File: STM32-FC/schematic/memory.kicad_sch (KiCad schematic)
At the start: 9 parts, among them J4 TF-06A, U5 W25X40CLUXIG

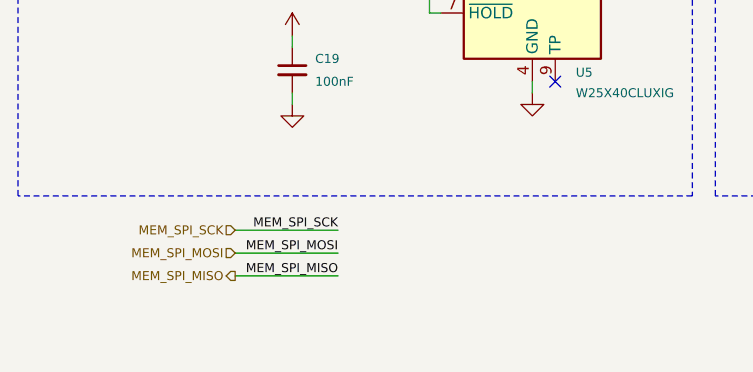
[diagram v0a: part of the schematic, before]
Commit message: v1.0.1 update WIP
repactor and USB C bug fix
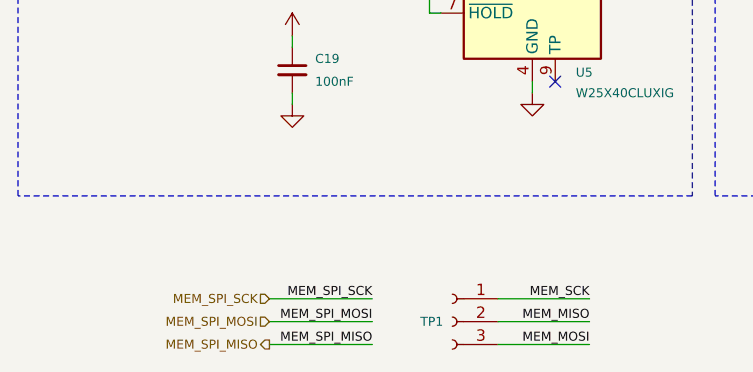
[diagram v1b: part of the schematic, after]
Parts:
- added TP1: Test Pin, Connector_PinHeader_1.27mm:PinHeader_1x03_P1.27mm_Vertical, symbol Connector:Conn_01x03_Socket
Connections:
- new net MEM_MISO: TP1.2 (Pin_2)
- new net MEM_MOSI: TP1.3 (Pin_3)
- new net MEM_SCK: TP1.1 (Pin_1)

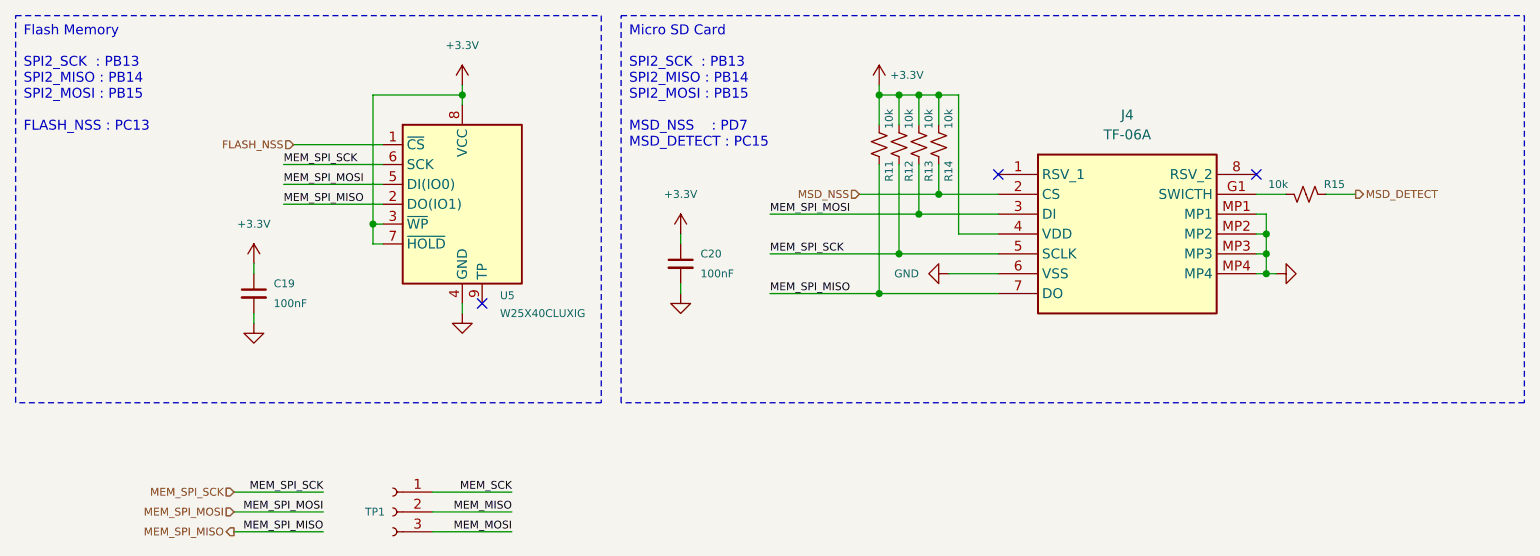
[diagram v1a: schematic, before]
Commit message: schematic update & lib update
- ICM-45686
- ICP-20100
- Micro SD update SDIO instead of SPI
- servo main output
- DC2DC buck instead power regulator
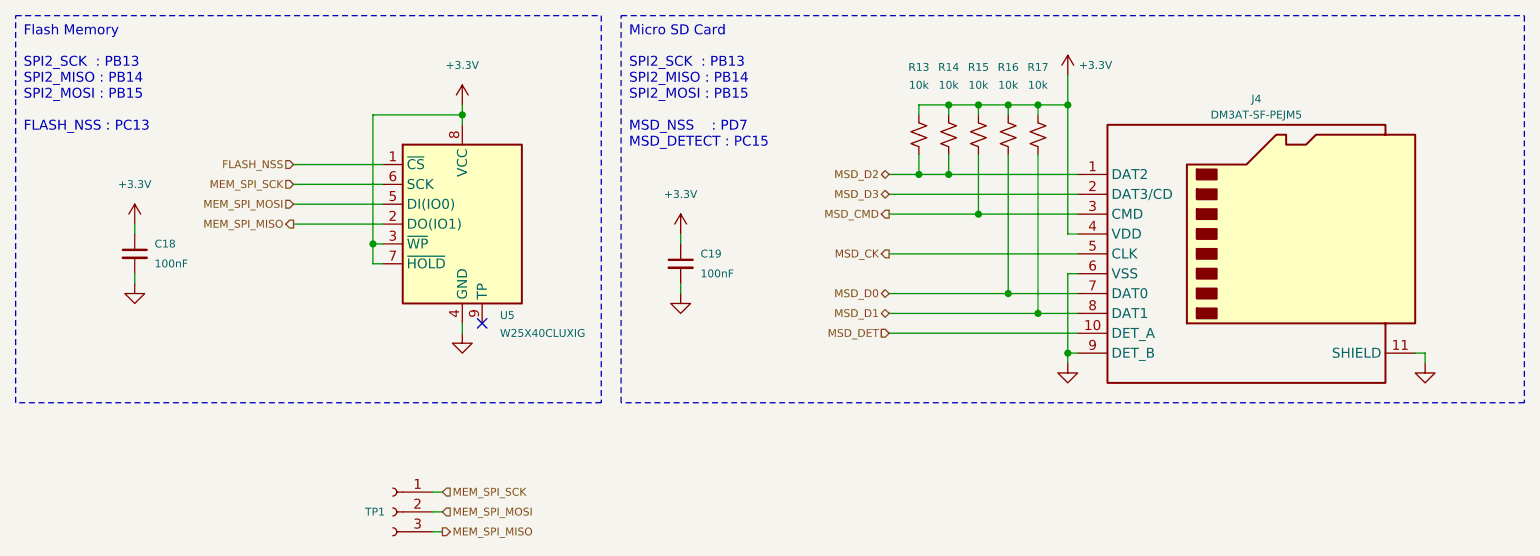
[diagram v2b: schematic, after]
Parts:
- removed J4: TF-06A, TF06A, symbol TF-06A:TF-06A
- removed R11, R12: 10k, Resistor_SMD:R_0402_1005Metric, symbol Device:R_Small_US
- added J4: DM3AT-SF-PEJM5, Connector_Card:microSD_HC_Hirose_DM3AT-SF-PEJM5, symbol Connector:Micro_SD_Card_Det2
- added R16, R17: 10k, Resistor_SMD:R_0402_1005Metric, symbol Device:R_Small_US
- U5: footprint W25X40CLUX:USON_LUXIG TR_WIN-L -> W25X40CLUX:USON_LUXIG_TR_HandSolder
- renumbered C19 to C18, C20 to C19
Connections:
- net MEM_MISO is gone; now on net MEM_SPI_MOSI: TP1.2 (Pin_2)
- net MEM_MOSI is gone; now on net MEM_SPI_MISO: TP1.3 (Pin_3)
- net MEM_SCK is gone; now on net MEM_SPI_SCK: TP1.1 (Pin_1)
- net MSD_DETECT is gone; now on net +3.3V: R15.1
- net +3.3V: now also J4.4 (VDD), R16.1, R17.1
- net GND: now also J4.11 (SHIELD), J4.6 (VSS), J4.9 (DET_B)
- net MEM_SPI_MOSI: no longer R13.2
- net MSD_CMD: now reaches R15.2
- net MSD_CMD: now also J4.3 (CMD)
- net MSD_NSS renamed MSD_D2
- net MSD_D2: now also R13.2, J4.1 (DAT2)
- new net MSD_CK: J4.5 (CLK)
- new net MSD_D0: J4.7 (DAT0), R16.2
- new net MSD_D1: J4.8 (DAT1), R17.2
- new net MSD_D3: J4.2 (DAT3/CD)
- new net MSD_DET: J4.10 (DET_A)
- no-connect marks 3 -> 1
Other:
- title: STM32 Flight Controller -> NARAEON - Flight Controller
- moved on the sheet: C18, U5

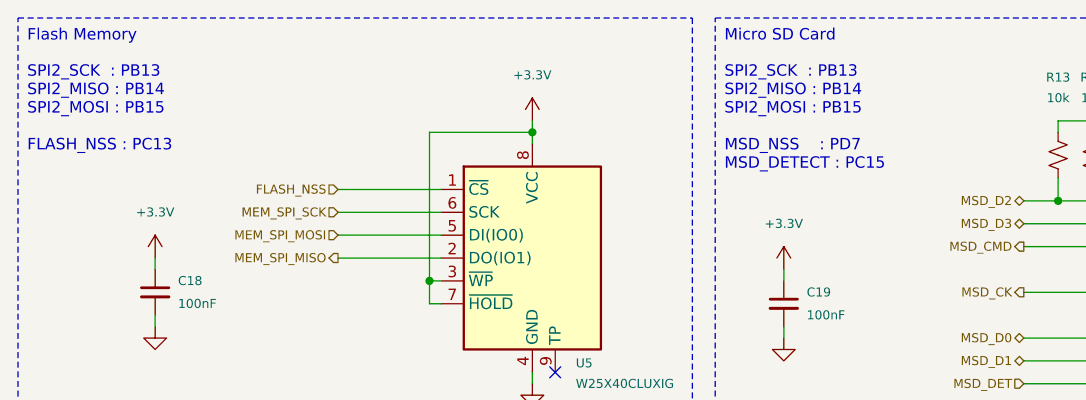
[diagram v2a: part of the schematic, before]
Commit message: add: servo power & comment
- Servo power diode add
- comment update
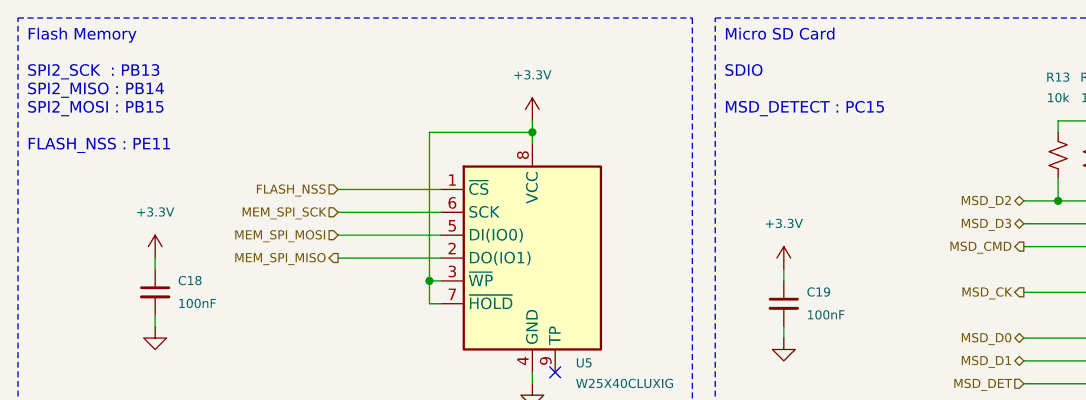
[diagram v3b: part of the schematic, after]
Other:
- note added: "SDIO MSD_DETECT : PC15"
- note added: "SPI2_SCK : PB13 SPI2_MISO : PB14 SPI2_MOSI : PB15 FLASH_NSS : PE11"
- note removed: "SPI2_SCK : PB13 SPI2_MISO : PB14 SPI2_MOSI : PB15 FLASH_NSS : PC13"
- note removed: "SPI2_SCK : PB13 SPI2_MISO : PB14 SPI2_MOSI : PB15 MSD_NSS : PD7 MSD_DETECT : PC15"
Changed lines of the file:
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@@
 	(title_block
 		(title "NARAEON - Flight Controller")
-		(date "2025-10-09")
+		(date "2025-10-10")
 		(rev "v1.1.0")
 		(company "NARAE")
@@
 		)
 	)
-	(text "SPI2_SCK  : PB13\nSPI2_MISO : PB14\nSPI2_MOSI : PB15\n\nMSD_NSS    : PD7\nMSD_DETECT : PC15"
+	(text "SDIO\n\nMSD_DETECT : PC15"
 		(exclude_from_sim no)
 		(at 101.346 18.034 0)
@@
 		)
 	)
-	(text "SPI2_SCK  : PB13\nSPI2_MISO : PB14\nSPI2_MOSI : PB15\n\nFLASH_NSS : PC13"
+	(text "SPI2_SCK  : PB13\nSPI2_MISO : PB14\nSPI2_MOSI : PB15\n\nFLASH_NSS : PE11"
 		(exclude_from_sim no)
 		(at 23.876 18.034 0)
@@
 		(dnp no)
 		(fields_autoplaced yes)
-		(property "Reference" "#PWR050"
+		(property "Reference" "#PWR053"
 			(at 157.48 63.5 0)
 			(effects
@@
 			(project "STM32-FC"
 				(path "/8d4cc317-3933-4aa6-844b-8c5c635e89c7/3e7c6c79-bc31-4cc9-af6a-d0a28245a7b2"
-					(reference "#PWR050")
+					(reference "#PWR053")
 					(unit 1)
 				)
@@
 		(dnp no)
 		(fields_autoplaced yes)
-		(property "Reference" "#PWR043"
+		(property "Reference" "#PWR046"
 			(at 38.1 43.18 0)
 			(effects
@@
 			(project "STM32-FC"
 				(path "/8d4cc317-3933-4aa6-844b-8c5c635e89c7/3e7c6c79-bc31-4cc9-af6a-d0a28245a7b2"
-					(reference "#PWR043")
+					(reference "#PWR046")
 					(unit 1)
 				)
@@
 		(dnp no)
 		(fields_autoplaced yes)
-		(property "Reference" "#PWR048"
+		(property "Reference" "#PWR051"
 			(at 107.95 54.61 0)
 			(effects
@@
 			(project "STM32-FC"
 				(path "/8d4cc317-3933-4aa6-844b-8c5c635e89c7/3e7c6c79-bc31-4cc9-af6a-d0a28245a7b2"
-					(reference "#PWR048")
+					(reference "#PWR051")
 					(unit 1)
 				)
@@
 		(dnp no)
 		(fields_autoplaced yes)
-		(property "Reference" "#PWR044"
+		(property "Reference" "#PWR047"
 			(at 38.1 53.34 0)
 			(effects
@@
 			(project "STM32-FC"
 				(path "/8d4cc317-3933-4aa6-844b-8c5c635e89c7/3e7c6c79-bc31-4cc9-af6a-d0a28245a7b2"
-					(reference "#PWR044")
+					(reference "#PWR047")
 					(unit 1)
 				)
@@
 		(dnp no)
 		(fields_autoplaced yes)
-		(property "Reference" "#PWR051"
+		(property "Reference" "#PWR054"
 			(at 203.2 63.5 0)
 			(effects
@@
 			(project "STM32-FC"
 				(path "/8d4cc317-3933-4aa6-844b-8c5c635e89c7/3e7c6c79-bc31-4cc9-af6a-d0a28245a7b2"
-					(reference "#PWR051")
+					(reference "#PWR054")
 					(unit 1)
 				)
@@
 		(dnp no)
 		(fields_autoplaced yes)
-		(property "Reference" "#PWR047"
+		(property "Reference" "#PWR050"
 			(at 107.95 44.45 0)
 			(effects
@@
 			(project "STM32-FC"
 				(path "/8d4cc317-3933-4aa6-844b-8c5c635e89c7/3e7c6c79-bc31-4cc9-af6a-d0a28245a7b2"
-					(reference "#PWR047")
+					(reference "#PWR050")
 					(unit 1)
 				)
@@
 		(on_board yes)
 		(dnp no)
-		(property "Reference" "#PWR049"
+		(property "Reference" "#PWR052"
 			(at 157.48 24.13 0)
 			(effects
@@
 			(project "STM32-FC"
 				(path "/8d4cc317-3933-4aa6-844b-8c5c635e89c7/3e7c6c79-bc31-4cc9-af6a-d0a28245a7b2"
-					(reference "#PWR049")
+					(reference "#PWR052")
 					(unit 1)
 				)
@@
 		(dnp no)
 		(fields_autoplaced yes)
-		(property "Reference" "#PWR045"
+		(property "Reference" "#PWR048"
 			(at 80.01 27.94 0)
 			(effects
@@
 			(project "STM32-FC"
 				(path "/8d4cc317-3933-4aa6-844b-8c5c635e89c7/3e7c6c79-bc31-4cc9-af6a-d0a28245a7b2"
-					(reference "#PWR045")
+					(reference "#PWR048")
 					(unit 1)
 				)
@@
 		(dnp no)
 		(fields_autoplaced yes)
-		(property "Reference" "#PWR046"
+		(property "Reference" "#PWR049"
 			(at 80.01 59.69 0)
 			(effects
@@
 			(project "STM32-FC"
 				(path "/8d4cc317-3933-4aa6-844b-8c5c635e89c7/3e7c6c79-bc31-4cc9-af6a-d0a28245a7b2"
-					(reference "#PWR046")
+					(reference "#PWR049")
 					(unit 1)
 				)

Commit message: WIP : pcb part layout &* BOM udpate
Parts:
- U5: footprint W25X40CLUX:USON_LUXIG_TR_HandSolder -> W25X40CLUX:USON_LUXIG TR_WIN
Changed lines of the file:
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@@
 			)
 		)
-		(property "Footprint" "W25X40CLUX:USON_LUXIG_TR_HandSolder"
+		(property "Footprint" "W25X40CLUX:USON_LUXIG TR_WIN"
 			(at 80.01 39.37 0)
 			(effects
@@
 			)
 		)
-		(property "Datasheet" "kicad-embed://w25x40cl_f 20140325.pdf"
+		(property "Datasheet" ""
 			(at 80.01 39.37 0)
 			(effects

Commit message: update : AHRS PCB layout & routing done
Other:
- note added: "SPI3_SCK : PB3 SPI3_MISO : PB4 SPI3_MOSI : PB5 FLASH_NSS : PE11"
- note removed: "SPI2_SCK : PB13 SPI2_MISO : PB14 SPI2_MOSI : PB15 FLASH_NSS : PE11"
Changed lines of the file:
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@@
 		(company "NARAE")
 		(comment 1 "INHA Univ. Areo-modelling Club")
-		(comment 2 "2024 Winter UAV Project ")
+		(comment 2 "* Work in progress")
 	)
 	(rectangle
@@
 		)
 	)
-	(text "SPI2_SCK  : PB13\nSPI2_MISO : PB14\nSPI2_MOSI : PB15\n\nFLASH_NSS : PE11"
+	(text "SPI3_SCK  : PB3\nSPI3_MISO : PB4\nSPI3_MOSI : PB5\n\nFLASH_NSS : PE11"
 		(exclude_from_sim no)
 		(at 23.876 18.034 0)

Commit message: PCB layout done
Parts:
- added R19: 10k, Resistor_SMD:R_0402_1005Metric, symbol Device:R_Small_US
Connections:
- net +3.3V: now also R19.1
- net MSD_D2: no longer R14.2
- net MSD_D3: now also R14.2
- net MSD_DET: now also R19.2
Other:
- moved on the sheet: R13, R14, R15, R16, R17

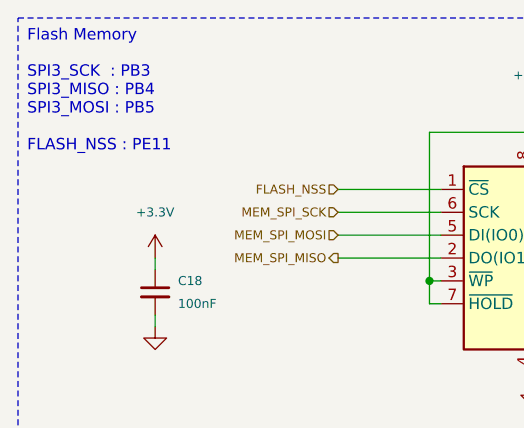
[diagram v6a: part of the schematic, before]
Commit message: fix : readme & schematic minor fix
- schematic comment fix
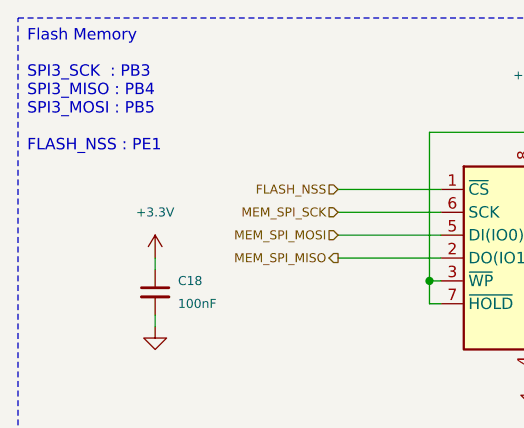
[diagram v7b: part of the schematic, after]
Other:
- note added: "SPI3_SCK : PB3 SPI3_MISO : PB4 SPI3_MOSI : PB5 FLASH_NSS : PE1"
- note removed: "SPI3_SCK : PB3 SPI3_MISO : PB4 SPI3_MOSI : PB5 FLASH_NSS : PE11"
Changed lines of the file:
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@@
 	(title_block
 		(title "NARAEON - Flight Controller")
-		(date "2025-10-10")
+		(date "2025-10-11")
 		(rev "v1.1.0")
 		(company "NARAE")
 		(comment 1 "INHA Univ. Areo-modelling Club")
-		(comment 2 "* Work in progress")
+		(comment 2 "github.com/NARAE-INHA-UNIV")
 	)
 	(rectangle
@@
 		)
 	)
-	(text "SPI3_SCK  : PB3\nSPI3_MISO : PB4\nSPI3_MOSI : PB5\n\nFLASH_NSS : PE11"
+	(text "SPI3_SCK  : PB3\nSPI3_MISO : PB4\nSPI3_MOSI : PB5\n\nFLASH_NSS : PE1"
 		(exclude_from_sim no)
 		(at 23.876 18.034 0)
